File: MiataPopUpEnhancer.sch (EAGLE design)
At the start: 84 parts, among them J3 USB4110-GF-A, Q1 MICRO_COMMERCIAL_MMSS8050-L-T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, Q11 MICRO_COMMERCIAL_MMSS8050-L-T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, Q12 MICRO_COMMERCIAL_MMSS8050-L-T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, Q13 DIODES_INC_DMP3099L-13DIODES_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, Q2 MICRO_COMMERCIAL_MMSS8050-L-T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, Q21 MICRO_COMMERCIAL_MMSS8050-L-T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, Q22 MICRO_COMMERCIAL_MMSS8050-L-T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, Q23 DIODES_INC_DMP3099L-13DIODES_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, Q3 DIODES_INC_DMP3099L-13DIODES_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, Q31 MICRO_COMMERCIAL_MMSS8050-L-T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, Q32 MICRO_COMMERCIAL_MMSS8050-L-T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, Q33 DIODES_INC_DMP3099L-13DIODES_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, SW1 KMR2, U1 ATSAMD21E18A-MUT, U2 MCP1703CB, U3 MDBT40, Y1 ABS25-32.768KHZ-T

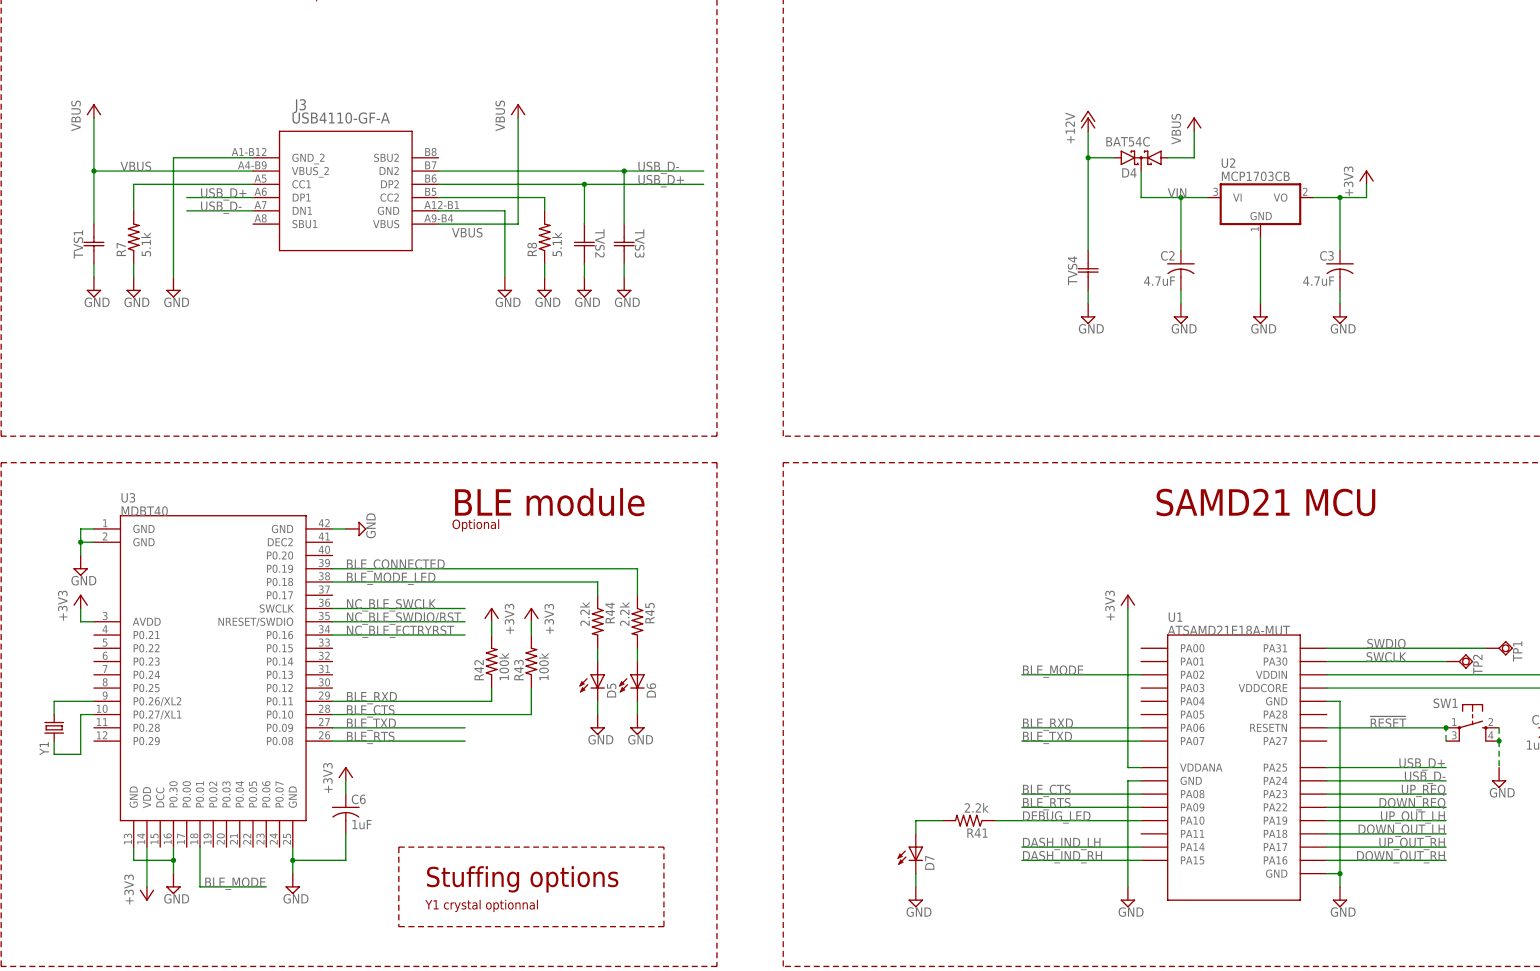
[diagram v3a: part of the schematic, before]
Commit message: First complete layout. Still using headers for connectors
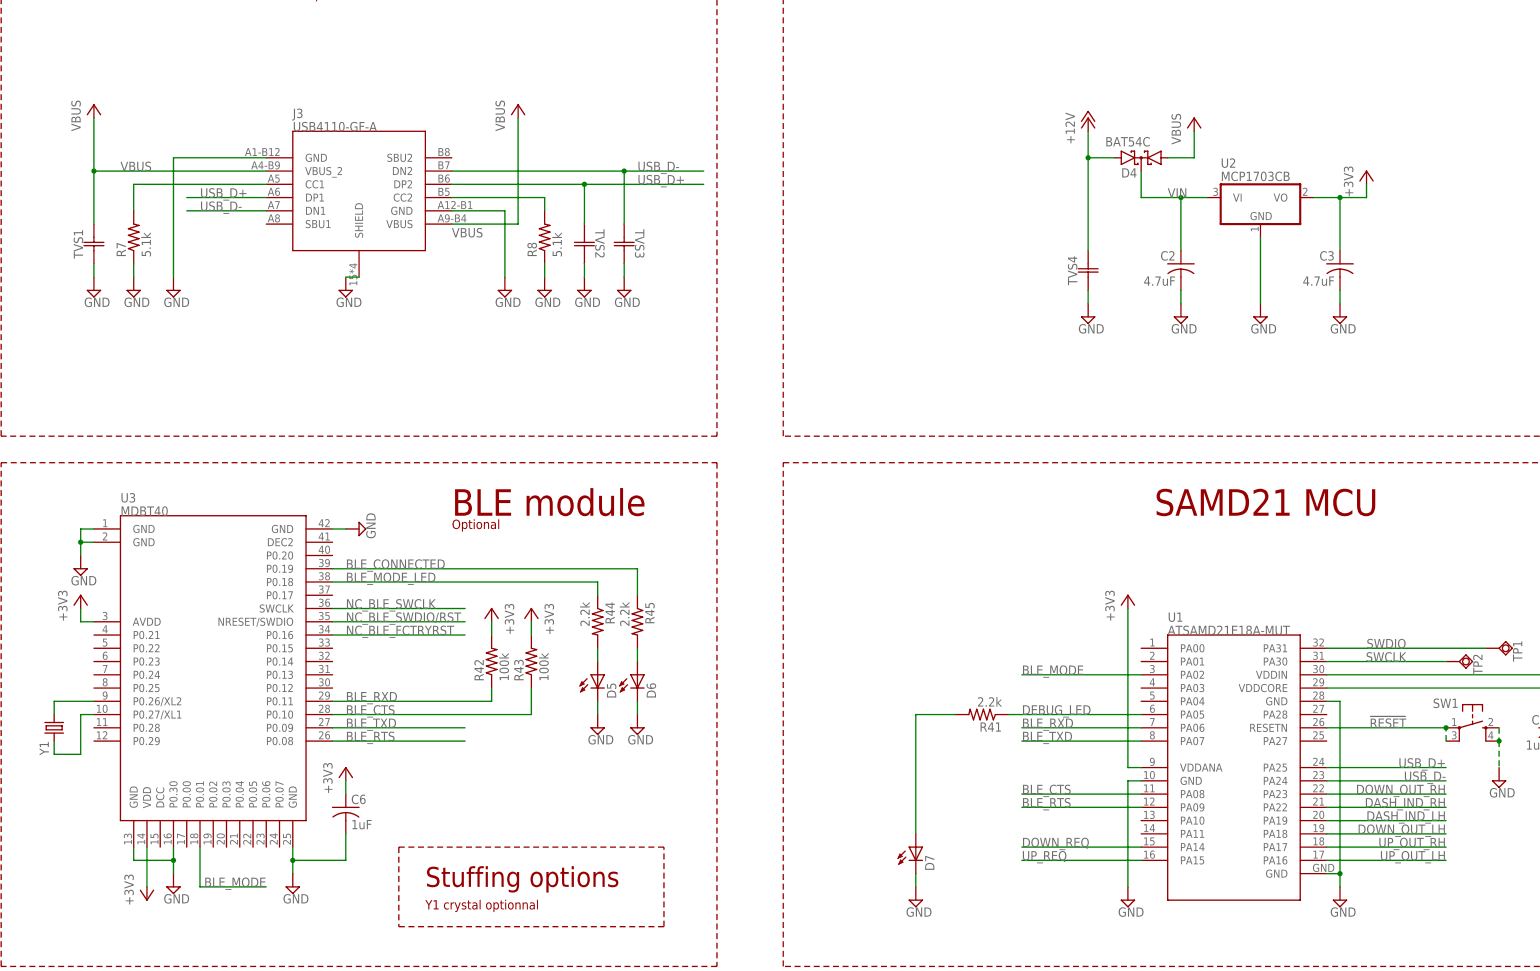
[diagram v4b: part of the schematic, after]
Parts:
- C2: device adafruit:C-USC0603 -> adafruit:C-USC0603K
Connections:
- net DASH_IND_LH: now also U1.PA19; no longer U1.PA14
- net DASH_IND_RH: now also U1.PA22; no longer U1.PA15
- net DEBUG_LED: now also U1.PA05; no longer U1.PA10
- net DOWN_OUT_RH: now also U1.PA23; no longer U1.PA16
- net DOWN_REQ: now also U1.PA14; no longer U1.PA22
- net GND: now also J3.GND@1, J3.GND@2, J3.SHIELD; no longer J3.GND, J3.GND_2
- net UP_OUT_LH: now also U1.PA16; no longer U1.PA19
- net UP_REQ: now also U1.PA15; no longer U1.PA23
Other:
- moved on the sheet: R41
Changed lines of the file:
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@@
 <part name="SUPPLY15" library="supply2" library_urn="urn:adsk.eagle:library:372" deviceset="GND" device=""/>
 <part name="+3V1" library="supply1" library_urn="urn:adsk.eagle:library:371" deviceset="+3V3" device=""/>
-<part name="C2" library="adafruit" deviceset="C-US" device="C0603" value="4.7uF"/>
+<part name="C2" library="adafruit" deviceset="C-US" device="C0603K" value="4.7uF"/>
 <part name="C3" library="adafruit" deviceset="C-US" device="C0603" value="4.7uF"/>
 <part name="SUPPLY16" library="supply2" library_urn="urn:adsk.eagle:library:372" deviceset="GND" device=""/>
@@
 <part name="D33" library="diode" library_urn="urn:adsk.eagle:library:210" deviceset="BZX84CSMD" device="" package3d_urn="urn:adsk.eagle:package:43403/2" value="3.3V"/>
 <part name="SUPPLY52" library="supply2" library_urn="urn:adsk.eagle:library:372" deviceset="GND" device=""/>
+<part name="SUPPLY53" library="supply2" library_urn="urn:adsk.eagle:library:372" deviceset="GND" device=""/>
 </parts>
 <sheets>
@@
 <attribute name="VALUE" x="280.035" y="19.685" size="1.778" layer="96"/>
 </instance>
-<instance part="J3" gate="A" x="30.48" y="142.24" smashed="yes">
-<attribute name="NAME" x="40.9956" y="151.3586" size="2.0828" layer="95" ratio="6" rot="SR0"/>
-<attribute name="VALUE" x="40.3606" y="148.8186" size="2.0828" layer="96" ratio="6" rot="SR0"/>
+<instance part="J3" gate="A" x="53.34" y="137.16" smashed="yes">
+<attribute name="NAME" x="40.64" y="149.86" size="1.778" layer="95" ratio="6" rot="SR0"/>
+<attribute name="VALUE" x="40.64" y="147.32" size="1.778" layer="96" ratio="6" rot="SR0"/>
 </instance>
 <instance part="SUPPLY22" gate="GND" x="81.28" y="116.84" smashed="yes">
@@
 <attribute name="VALUE" x="290.195" y="19.685" size="1.778" layer="96"/>
 </instance>
-<instance part="R41" gate="G$1" x="170.18" y="15.24" smashed="yes" rot="R180">
-<attribute name="NAME" x="173.99" y="13.7414" size="1.778" layer="95" rot="R180"/>
-<attribute name="VALUE" x="173.99" y="18.542" size="1.778" layer="96" rot="R180"/>
+<instance part="R41" gate="G$1" x="172.72" y="35.56" smashed="yes" rot="R180">
+<attribute name="NAME" x="176.53" y="34.0614" size="1.778" layer="95" rot="R180"/>
+<attribute name="VALUE" x="176.53" y="38.862" size="1.778" layer="96" rot="R180"/>
 </instance>
 <instance part="D7" gate="G$1" x="160.02" y="10.16" smashed="yes">
@@
 <instance part="SUPPLY52" gate="GND" x="68.58" y="-271.78" smashed="yes">
 <attribute name="VALUE" x="66.675" y="-274.955" size="1.778" layer="96"/>
+</instance>
+<instance part="SUPPLY53" gate="GND" x="50.8" y="116.84" smashed="yes">
+<attribute name="VALUE" x="48.895" y="113.665" size="1.778" layer="96"/>
 </instance>
 </instances>
@@
 </segment>
 <segment>
-<pinref part="J3" gate="A" pin="GND"/>
-<wire x1="68.58" y1="132.08" x2="81.28" y2="132.08" width="0.1524" layer="91"/>
+<pinref part="J3" gate="A" pin="GND@1"/>
+<wire x1="71.12" y1="132.08" x2="81.28" y2="132.08" width="0.1524" layer="91"/>
 <wire x1="81.28" y1="132.08" x2="81.28" y2="119.38" width="0.1524" layer="91"/>
 <pinref part="SUPPLY22" gate="GND" pin="GND"/>
 </segment>
 <segment>
-<pinref part="J3" gate="A" pin="GND_2"/>
-<wire x1="33.02" y1="142.24" x2="17.78" y2="142.24" width="0.1524" layer="91"/>
+<pinref part="J3" gate="A" pin="GND@2"/>
+<wire x1="35.56" y1="142.24" x2="17.78" y2="142.24" width="0.1524" layer="91"/>
 <wire x1="17.78" y1="142.24" x2="17.78" y2="119.38" width="0.1524" layer="91"/>
 <pinref part="SUPPLY23" gate="GND" pin="GND"/>
@@
 <wire x1="68.58" y1="-269.24" x2="68.58" y2="-266.7" width="0.1524" layer="91"/>
 </segment>
+<segment>
+<pinref part="J3" gate="A" pin="SHIELD"/>
+<pinref part="SUPPLY53" gate="GND" pin="GND"/>
+<wire x1="50.8" y1="119.38" x2="53.34" y2="119.38" width="0.1524" layer="91"/>
+</segment>
 </net>
 <net name="+12V" class="0">
@@
 </segment>
 <segment>
-<wire x1="238.76" y1="15.24" x2="261.62" y2="15.24" width="0.1524" layer="91"/>
-<label x="261.62" y="15.24" size="1.778" layer="95" rot="MR0"/>
-<pinref part="U1" gate="G$1" pin="PA19"/>
+<wire x1="238.76" y1="7.62" x2="261.62" y2="7.62" width="0.1524" layer="91"/>
+<label x="261.62" y="7.62" size="1.778" layer="95" rot="MR0"/>
+<pinref part="U1" gate="G$1" pin="PA16"/>
 </segment>
 </net>
@@
 </segment>
 <segment>
-<wire x1="238.76" y1="20.32" x2="261.62" y2="20.32" width="0.1524" layer="91"/>
-<label x="261.62" y="20.32" size="1.778" layer="95" rot="MR0"/>
-<pinref part="U1" gate="G$1" pin="PA23"/>
+<pinref part="U1" gate="G$1" pin="PA15"/>
+<wire x1="203.2" y1="7.62" x2="180.34" y2="7.62" width="0.1524" layer="91"/>
+<label x="180.34" y="7.62" size="1.778" layer="95"/>
 </segment>
 </net>
@@
 </segment>
 <segment>
-<wire x1="261.62" y1="17.78" x2="238.76" y2="17.78" width="0.1524" layer="91"/>
-<label x="261.62" y="17.78" size="1.778" layer="95" rot="MR0"/>
-<pinref part="U1" gate="G$1" pin="PA22"/>
+<pinref part="U1" gate="G$1" pin="PA14"/>
+<wire x1="180.34" y1="10.16" x2="203.2" y2="10.16" width="0.1524" layer="91"/>
+<label x="180.34" y="10.16" size="1.778" layer="95"/>
 </segment>
 </net>
@@
 </segment>
 <segment>
-<wire x1="33.02" y1="132.08" x2="20.32" y2="132.08" width="0.1524" layer="91"/>
+<wire x1="35.56" y1="132.08" x2="20.32" y2="132.08" width="0.1524" layer="91"/>
 <pinref part="J3" gate="A" pin="DN1"/>
 <label x="22.86" y="132.08" size="1.778" layer="95"/>
@@
 <wire x1="119.38" y1="139.7" x2="104.14" y2="139.7" width="0.1524" layer="91"/>
 <pinref part="TVS3" gate="A" pin="2"/>
-<wire x1="104.14" y1="139.7" x2="68.58" y2="139.7" width="0.1524" layer="91"/>
+<wire x1="104.14" y1="139.7" x2="71.12" y2="139.7" width="0.1524" layer="91"/>
 <wire x1="104.14" y1="129.54" x2="104.14" y2="139.7" width="0.1524" layer="91"/>
 <junction x="104.14" y="139.7"/>
@@
 <segment>
 <pinref part="J3" gate="A" pin="DP1"/>
-<wire x1="33.02" y1="134.62" x2="20.32" y2="134.62" width="0.1524" layer="91"/>
+<wire x1="35.56" y1="134.62" x2="20.32" y2="134.62" width="0.1524" layer="91"/>
 <label x="22.86" y="134.62" size="1.778" layer="95"/>
 </segment>
@@
 <pinref part="J3" gate="A" pin="DP2"/>
 <label x="106.68" y="137.16" size="1.778" layer="95"/>
-<wire x1="68.58" y1="137.16" x2="96.52" y2="137.16" width="0.1524" layer="91"/>
+<wire x1="71.12" y1="137.16" x2="96.52" y2="137.16" width="0.1524" layer="91"/>
 <pinref part="TVS2" gate="A" pin="2"/>
 <wire x1="96.52" y1="137.16" x2="119.38" y2="137.16" width="0.1524" layer="91"/>
@@
 <segment>
 <pinref part="J3" gate="A" pin="VBUS_2"/>
-<wire x1="33.02" y1="139.7" x2="2.54" y2="139.7" width="0.1524" layer="91"/>
+<wire x1="35.56" y1="139.7" x2="2.54" y2="139.7" width="0.1524" layer="91"/>
 <wire x1="2.54" y1="139.7" x2="2.54" y2="149.86" width="0.1524" layer="91"/>
 <pinref part="P+8" gate="1" pin="+5V"/>
@@
 <segment>
 <pinref part="J3" gate="A" pin="VBUS"/>
-<wire x1="68.58" y1="129.54" x2="83.82" y2="129.54" width="0.1524" layer="91"/>
+<wire x1="71.12" y1="129.54" x2="83.82" y2="129.54" width="0.1524" layer="91"/>
 <wire x1="83.82" y1="129.54" x2="83.82" y2="149.86" width="0.1524" layer="91"/>
 <pinref part="P+9" gate="1" pin="+5V"/>
@@
 <pinref part="J3" gate="A" pin="CC1"/>
 <wire x1="10.16" y1="132.08" x2="10.16" y2="137.16" width="0.1524" layer="91"/>
-<wire x1="10.16" y1="137.16" x2="33.02" y2="137.16" width="0.1524" layer="91"/>
+<wire x1="10.16" y1="137.16" x2="35.56" y2="137.16" width="0.1524" layer="91"/>
 </segment>
 </net>
@@
 <pinref part="J3" gate="A" pin="CC2"/>
 <wire x1="88.9" y1="132.08" x2="88.9" y2="134.62" width="0.1524" layer="91"/>
-<wire x1="88.9" y1="134.62" x2="68.58" y2="134.62" width="0.1524" layer="91"/>
+<wire x1="88.9" y1="134.62" x2="71.12" y2="134.62" width="0.1524" layer="91"/>
 </segment>
 </net>
@@
 </segment>
 <segment>
-<wire x1="238.76" y1="7.62" x2="261.62" y2="7.62" width="0.1524" layer="91"/>
-<label x="261.62" y="7.62" size="1.778" layer="95" rot="MR0"/>
-<pinref part="U1" gate="G$1" pin="PA16"/>
+<wire x1="238.76" y1="20.32" x2="261.62" y2="20.32" width="0.1524" layer="91"/>
+<label x="261.62" y="20.32" size="1.778" layer="95" rot="MR0"/>
+<pinref part="U1" gate="G$1" pin="PA23"/>
 </segment>
 </net>
@@
 <net name="DEBUG_LED" class="0">
 <segment>
-<pinref part="U1" gate="G$1" pin="PA10"/>
-<wire x1="203.2" y1="15.24" x2="175.26" y2="15.24" width="0.1524" layer="91"/>
-<label x="180.34" y="15.24" size="1.778" layer="95"/>
+<pinref part="U1" gate="G$1" pin="PA05"/>
+<wire x1="203.2" y1="35.56" x2="177.8" y2="35.56" width="0.1524" layer="91"/>
+<label x="180.34" y="35.56" size="1.778" layer="95"/>
 <pinref part="R41" gate="G$1" pin="1"/>
 </segment>
@@
 <pinref part="R41" gate="G$1" pin="2"/>
 <pinref part="D7" gate="G$1" pin="A"/>
-<wire x1="165.1" y1="15.24" x2="160.02" y2="15.24" width="0.1524" layer="91"/>
-<wire x1="160.02" y1="15.24" x2="160.02" y2="12.7" width="0.1524" layer="91"/>
+<wire x1="167.64" y1="35.56" x2="160.02" y2="35.56" width="0.1524" layer="91"/>
+<wire x1="160.02" y1="35.56" x2="160.02" y2="12.7" width="0.1524" layer="91"/>
 </segment>
 </net>
@@
 </segment>
 <segment>
-<pinref part="U1" gate="G$1" pin="PA14"/>
-<wire x1="180.34" y1="10.16" x2="203.2" y2="10.16" width="0.1524" layer="91"/>
-<label x="180.34" y="10.16" size="1.778" layer="95"/>
+<wire x1="238.76" y1="15.24" x2="261.62" y2="15.24" width="0.1524" layer="91"/>
+<label x="261.62" y="15.24" size="1.778" layer="95" rot="MR0"/>
+<pinref part="U1" gate="G$1" pin="PA19"/>
 </segment>
 </net>
@@
 </segment>
 <segment>
-<pinref part="U1" gate="G$1" pin="PA15"/>
-<wire x1="203.2" y1="7.62" x2="180.34" y2="7.62" width="0.1524" layer="91"/>
-<label x="180.34" y="7.62" size="1.778" layer="95"/>
+<wire x1="261.62" y1="17.78" x2="238.76" y2="17.78" width="0.1524" layer="91"/>
+<label x="261.62" y="17.78" size="1.778" layer="95" rot="MR0"/>
+<pinref part="U1" gate="G$1" pin="PA22"/>
 </segment>
 </net>
@@
 </sheet>
 </sheets>
+<errors>
+</errors>
 </schematic>
 </drawing>
